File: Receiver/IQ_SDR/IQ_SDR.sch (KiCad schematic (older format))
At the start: 97 parts, among them CON1 SJ1-3523N, J1 ANT, J10 LO_I, J11 LO_Q, J12 GNDA, J13 I_IN, J14 Q_IN, J15 +5V, J16 4.3V, J17 I_OUT, J18 Q_OUT, J19 Conn_01x01_Male, J2 GND, J20 Conn_01x01_Male, J3 V_IN pin header, J4 GND, J5 V_IN, J6 FIL_O, J7 CLK1, J8 CLK2, J9 CLK0, P1 BNC, P2 SMA, Q1 MMBT2222A-TP, T1 Transformer_1P_SS, U1 FST3253 or TS3A5017, U2 Si5351A-B-GT, U3 TS5A23157, U4 LM4562 or LT6231, U5 74ALVC74D, Y1 CX3225

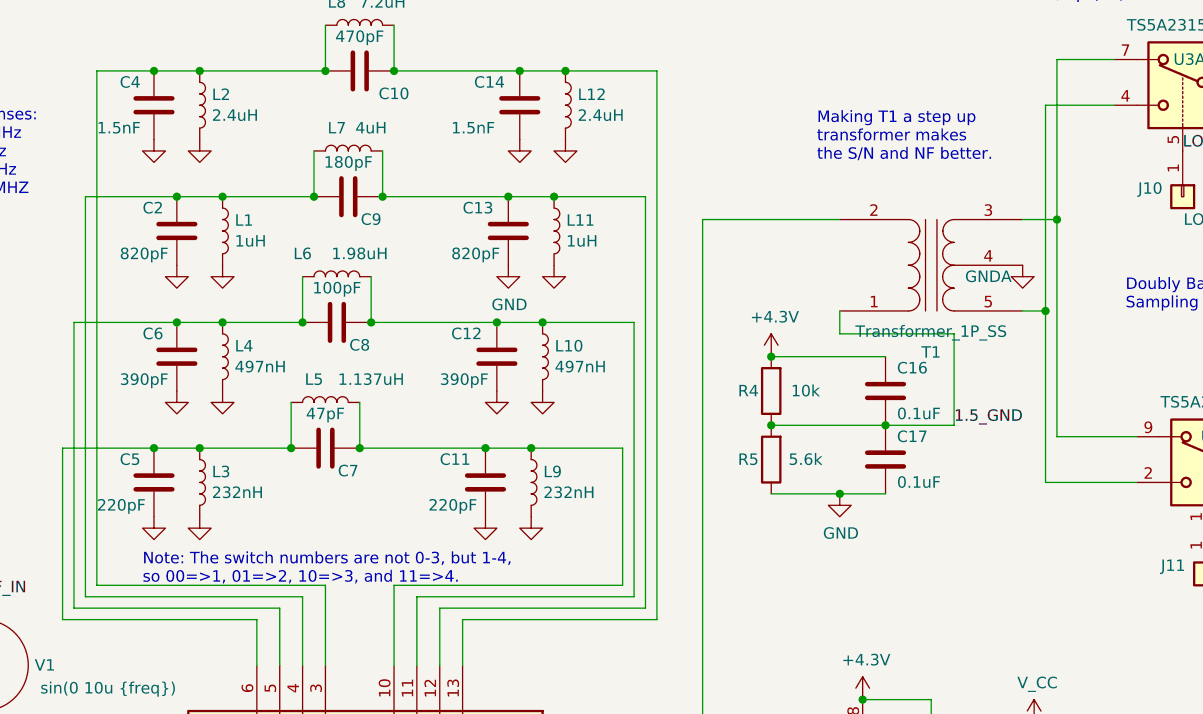
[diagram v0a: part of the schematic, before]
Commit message: Fixes to band pass filters, and notes to help with software.
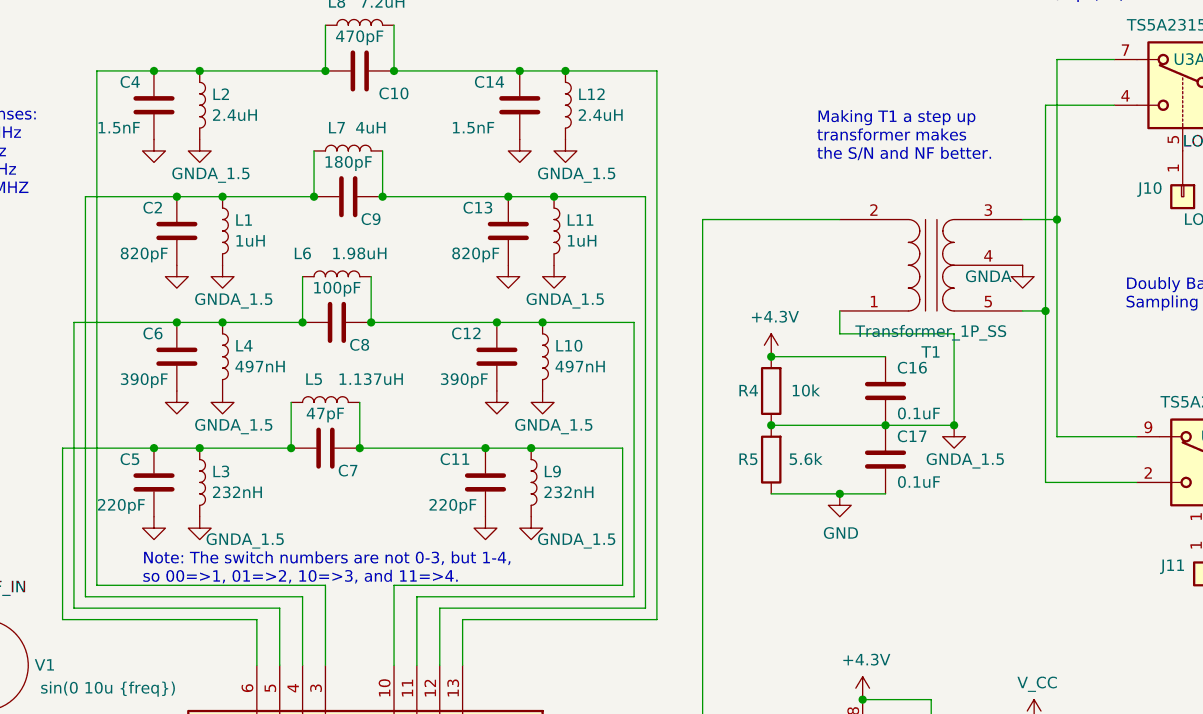
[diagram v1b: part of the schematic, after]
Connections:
- net 1.5_GND is gone; now on net GNDA: C16.2, C17.1, R4.1, R5.2, T1.1 (AA)
- net GND: no longer L1.2, L10.2, L11.2, L12.2, L2.2, L3.2, L4.2, L9.2
- net GNDA: now also L1.2, L10.2, L11.2, L12.2, L2.2, L3.2, L4.2, L9.2
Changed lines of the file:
@@
-$EndComp
-$Comp
-L IQ_SDR-rescue:GND-power #PWR016
-U 1 1 5D18958A
-P 2000 3900
-F 0 "#PWR016" H 2000 3650 50  0001 C CNN
-F 1 "GND" H 2005 3727 50  0001 C CNN
-F 2 "" H 2000 3900 50  0001 C CNN
-F 3 "" H 2000 3900 50  0001 C CNN
-	1    2000 3900
-	1    0    0    -1
 $EndComp
 $Comp
@@
 F 3 "" H 3400 3900 50  0001 C CNN
 	1    3400 3900
-	1    0    0    -1
-$EndComp
-$Comp
-L IQ_SDR-rescue:GND-power #PWR031
-U 1 1 5D189714
-P 3600 3900
-F 0 "#PWR031" H 3600 3650 50  0001 C CNN
-F 1 "GND" H 3605 3727 50  0001 C CNN
-F 2 "" H 3600 3900 50  0001 C CNN
-F 3 "" H 3600 3900 50  0001 C CNN
-	1    3600 3900
 	1    0    0    -1
 $EndComp
@@
 $EndComp
 $Comp
-L IQ_SDR-rescue:GND-power #PWR015
-U 1 1 5D1D4024
-P 2100 4450
-F 0 "#PWR015" H 2100 4200 50  0001 C CNN
-F 1 "GND" H 2105 4277 50  0001 C CNN
-F 2 "" H 2100 4450 50  0001 C CNN
-F 3 "" H 2100 4450 50  0001 C CNN
-	1    2100 4450
-	1    0    0    -1
-$EndComp
-$Comp
 L IQ_SDR-rescue:GND-power #PWR025
 U 1 1 5D1D402A
 P 3350 4450
 F 0 "#PWR025" H 3350 4200 50  0001 C CNN
-F 1 "GND" H 3355 4277 50  0000 C CNN
+F 1 "GND-power" H 3355 4277 50  0001 C CNN
 F 2 "" H 3350 4450 50  0001 C CNN
 F 3 "" H 3350 4450 50  0001 C CNN
 	1    3350 4450
-	1    0    0    -1
-$EndComp
-$Comp
-L IQ_SDR-rescue:GND-power #PWR030
-U 1 1 5D1D4030
-P 3550 4450
-F 0 "#PWR030" H 3550 4200 50  0001 C CNN
-F 1 "GND" H 3555 4277 50  0001 C CNN
-F 2 "" H 3550 4450 50  0001 C CNN
-F 3 "" H 3550 4450 50  0001 C CNN
-	1    3550 4450
 	1    0    0    -1
 $EndComp
@@
 $EndComp
 $Comp
-L IQ_SDR-rescue:GND-power #PWR018
-U 1 1 5D22E34C
-P 2100 5000
-F 0 "#PWR018" H 2100 4750 50  0001 C CNN
-F 1 "GND" H 2105 4827 50  0001 C CNN
-F 2 "" H 2100 5000 50  0001 C CNN
-F 3 "" H 2100 5000 50  0001 C CNN
-	1    2100 5000
-	1    0    0    -1
-$EndComp
-$Comp
 L IQ_SDR-rescue:GND-power #PWR024
 U 1 1 5D22E352
@@
 F 3 "" H 3300 5000 50  0001 C CNN
 	1    3300 5000
-	1    0    0    -1
-$EndComp
-$Comp
-L IQ_SDR-rescue:GND-power #PWR029
-U 1 1 5D22E358
-P 3500 5000
-F 0 "#PWR029" H 3500 4750 50  0001 C CNN
-F 1 "GND" H 3505 4827 50  0001 C CNN
-F 2 "" H 3500 5000 50  0001 C CNN
-F 3 "" H 3500 5000 50  0001 C CNN
-	1    3500 5000
 	1    0    0    -1
 $EndComp
@@
 $EndComp
 $Comp
-L IQ_SDR-rescue:GND-power #PWR017
-U 1 1 5D258FF6
-P 2000 5550
-F 0 "#PWR017" H 2000 5300 50  0001 C CNN
-F 1 "GND" H 2005 5377 50  0001 C CNN
-F 2 "" H 2000 5550 50  0001 C CNN
-F 3 "" H 2000 5550 50  0001 C CNN
-	1    2000 5550
-	1    0    0    -1
-$EndComp
-$Comp
 L IQ_SDR-rescue:GND-power #PWR023
 U 1 1 5D258FFC
@@
 F 3 "" H 3250 5550 50  0001 C CNN
 	1    3250 5550
-	1    0    0    -1
-$EndComp
-$Comp
-L IQ_SDR-rescue:GND-power #PWR027
-U 1 1 5D259002
-P 3450 5550
-F 0 "#PWR027" H 3450 5300 50  0001 C CNN
-F 1 "GND" H 3455 5377 50  0001 C CNN
-F 2 "" H 3450 5550 50  0001 C CNN
-F 3 "" H 3450 5550 50  0001 C CNN
-	1    3450 5550
 	1    0    0    -1
 $EndComp
@@
 Text Notes 1750 5850 0    50   ~ 0
 Note: The switch numbers are not 0-3, but 1-4,\nso 00=>1, 01=>2, 10=>3, and 11=>4.
-Text Label 5300 5150 0    50   ~ 0
-1.5_GND
 Text Notes 1700 3250 0    50   ~ 0
 Inductors in bandpass filters need to go to 1.5_GND, not GND.\nThey will short out the bias for the switches.
+$Comp
+L IQ_SDR-rescue:GNDA_1.5 #PWR?
+U 1 1 5DFD18B6
+P 3450 5550
+F 0 "#PWR?" H 3450 5300 50  0001 C CNN
+F 1 "GNDA_1.5" H 3650 5450 50  0000 C CNN
+F 2 "" H 3450 5550 50  0001 C CNN
+F 3 "" H 3450 5550 50  0001 C CNN
+	1    3450 5550
+	1    0    0    -1
+$EndComp
+$Comp
+L IQ_SDR-rescue:GNDA_1.5 #PWR?
+U 1 1 5DFD20EC
+P 2000 5550
+F 0 "#PWR?" H 2000 5300 50  0001 C CNN
+F 1 "GNDA_1.5" H 2200 5450 50  0000 C CNN
+F 2 "" H 2000 5550 50  0001 C CNN
+F 3 "" H 2000 5550 50  0001 C CNN
+	1    2000 5550
+	1    0    0    -1
+$EndComp
+$Comp
+L IQ_SDR-rescue:GNDA_1.5 #PWR?
+U 1 1 5DFD2615
+P 2100 5000
+F 0 "#PWR?" H 2100 4750 50  0001 C CNN
+F 1 "GNDA_1.5" H 2150 4850 50  0000 C CNN
+F 2 "" H 2100 5000 50  0001 C CNN
+F 3 "" H 2100 5000 50  0001 C CNN
+	1    2100 5000
+	1    0    0    -1
+$EndComp
+$Comp
+L IQ_SDR-rescue:GNDA_1.5 #PWR?
+U 1 1 5DFD2B56
+P 3500 5000
+F 0 "#PWR?" H 3500 4750 50  0001 C CNN
+F 1 "GNDA_1.5" H 3550 4850 50  0000 C CNN
+F 2 "" H 3500 5000 50  0001 C CNN
+F 3 "" H 3500 5000 50  0001 C CNN
+	1    3500 5000
+	1    0    0    -1
+$EndComp
+$Comp
+L IQ_SDR-rescue:GNDA_1.5 #PWR?
+U 1 1 5DFE0E2F
+P 3550 4450
+F 0 "#PWR?" H 3550 4200 50  0001 C CNN
+F 1 "GNDA_1.5" H 3600 4300 50  0000 C CNN
+F 2 "" H 3550 4450 50  0001 C CNN
+F 3 "" H 3550 4450 50  0001 C CNN
+	1    3550 4450
+	1    0    0    -1
+$EndComp
+$Comp
+L IQ_SDR-rescue:GNDA_1.5 #PWR?
+U 1 1 5DFE128D
+P 2100 4450
+F 0 "#PWR?" H 2100 4200 50  0001 C CNN
+F 1 "GNDA_1.5" H 2150 4300 50  0000 C CNN
+F 2 "" H 2100 4450 50  0001 C CNN
+F 3 "" H 2100 4450 50  0001 C CNN
+	1    2100 4450
+	1    0    0    -1
+$EndComp
+$Comp
+L IQ_SDR-rescue:GNDA_1.5 #PWR?
+U 1 1 5DFE192D
+P 3600 3900
+F 0 "#PWR?" H 3600 3650 50  0001 C CNN
+F 1 "GNDA_1.5" H 3650 3750 50  0000 C CNN
+F 2 "" H 3600 3900 50  0001 C CNN
+F 3 "" H 3600 3900 50  0001 C CNN
+	1    3600 3900
+	1    0    0    -1
+$EndComp
+$Comp
+L IQ_SDR-rescue:GNDA_1.5 #PWR?
+U 1 1 5DFE1C8B
+P 2000 3900
+F 0 "#PWR?" H 2000 3650 50  0001 C CNN
+F 1 "GNDA_1.5" H 2050 3750 50  0000 C CNN
+F 2 "" H 2000 3900 50  0001 C CNN
+F 3 "" H 2000 3900 50  0001 C CNN
+	1    2000 3900
+	1    0    0    -1
+$EndComp
+$Comp
+L IQ_SDR-rescue:GNDA_1.5 #PWR?
+U 1 1 5DFE2205
+P 5300 5150
+F 0 "#PWR?" H 5300 4900 50  0001 C CNN
+F 1 "GNDA_1.5" H 5350 5000 50  0000 C CNN
+F 2 "" H 5300 5150 50  0001 C CNN
+F 3 "" H 5300 5150 50  0001 C CNN
+	1    5300 5150
+	1    0    0    -1
+$EndComp
+Connection ~ 5300 5150
 $EndSCHEMATC

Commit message: Fixed R9-R12 and C26 and C26-C27 values
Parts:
- C26, C27: value 2200pF -> 440pF
- R10, R9: value 10 -> 51
- R11, R12: value 1.0k -> 5.1k
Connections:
- wire segments 216 -> 217
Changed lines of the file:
@@
 Title "Arduino HF SDR Receiver"
 Date "2019-07-11"
-Rev "0.1"
+Rev "0.11"
 Comp "Walla Walla University"
 Comment1 "Rob Frohne, KL7NA"
@@
 P 9550 1950
 F 0 "A1" H 9550 1900 50  0000 C CNN
-F 1 "Arduino_Nano_v3.x" H 9650 650 50  0000 C CNN
+F 1 "Arduino_Nano_v3.x" H 9550 2650 50  0000 C CNN
 F 2 "Modules:Arduino_Nano" H 9700 1000 50  0001 L CNN
 F 3 "https://www.arduino.cc/en/uploads/Main/Arduino_Nano-Rev3.2-SCH.pdf" H 9550 950 50  0001 C CNN
@@
 LO_Q
 $Comp
-L IQ_SDR-rescue:GNDA-power #PWR042
-U 1 1 5CF5C6F9
-P 5600 4450
-F 0 "#PWR042" H 5600 4200 50  0001 C CNN
-F 1 "GNDA" H 5450 4400 50  0000 C CNN
-F 2 "" H 5600 4450 50  0001 C CNN
-F 3 "" H 5600 4450 50  0001 C CNN
-	1    5600 4450
-	1    0    0    -1
-$EndComp
-$Comp
 L IQ_SDR-rescue:+3.3V-power #PWR040
 U 1 1 5CF636F6
@@
 $EndComp
 $Comp
-L IQ_SDR-rescue:GNDA-power #PWR055
-U 1 1 5D491346
-P 7750 4600
-F 0 "#PWR055" H 7750 4350 50  0001 C CNN
-F 1 "GNDA" H 7755 4427 50  0000 C CNN
-F 2 "" H 7750 4600 50  0001 C CNN
-F 3 "" H 7750 4600 50  0001 C CNN
-	1    7750 4600
-	1    0    0    -1
-$EndComp
-$Comp
 L IQ_SDR-rescue:GND-power #PWR053
 U 1 1 5CFD92C7
@@
 	7750 4600 7750 4250
 Wire Wire Line
-	7750 3850 8200 3850
+	7750 3850 7950 3850
 Connection ~ 7750 4250
-$Comp
-L IQ_SDR-rescue:GNDA-power #PWR059
-U 1 1 5D491349
-P 8200 5250
-F 0 "#PWR059" H 8200 5000 50  0001 C CNN
-F 1 "GNDA" H 8205 5077 50  0000 C CNN
-F 2 "" H 8200 5250 50  0001 C CNN
-F 3 "" H 8200 5250 50  0001 C CNN
-	1    8200 5250
-	1    0    0    -1
-$EndComp
 $Comp
 L IQ_SDR-rescue:C-Device C22
@@
 P 7900 5050
 F 0 "R10" V 7693 5050 50  0000 C CNN
-F 1 "10" V 7784 5050 50  0000 C CNN
+F 1 "51" V 7784 5050 50  0000 C CNN
 F 2 "Resistors_SMD:R_0805" V 7830 5050 50  0001 C CNN
 F 3 "~" H 7900 5050 50  0001 C CNN
@@
 P 8500 4700
 F 0 "R12" V 8293 4700 50  0000 C CNN
-F 1 "1.0k" V 8384 4700 50  0000 C CNN
+F 1 "5.1k" V 8384 4700 50  0000 C CNN
 F 2 "Resistors_SMD:R_0805" V 8430 4700 50  0001 C CNN
 F 3 "~" H 8500 4700 50  0001 C CNN
@@
 P 8500 4350
 F 0 "C27" V 8450 4500 50  0000 C CNN
-F 1 "2200pF" V 8350 4350 50  0000 C CNN
+F 1 "440pF" V 8350 4350 50  0000 C CNN
 F 2 "Capacitors_SMD:C_0805" H 8538 4200 50  0001 C CNN
 F 3 "~" H 8500 4350 50  0001 C CNN
@@
 P 7850 3650
 F 0 "R9" V 7643 3650 50  0000 C CNN
-F 1 "10" V 7734 3650 50  0000 C CNN
+F 1 "51" V 7734 3650 50  0000 C CNN
 F 2 "Resistors_SMD:R_0805" V 7780 3650 50  0001 C CNN
 F 3 "~" H 7850 3650 50  0001 C CNN
@@
 P 8500 3300
 F 0 "R11" V 8293 3300 50  0000 C CNN
-F 1 "1.0k" V 8384 3300 50  0000 C CNN
+F 1 "5.1k" V 8384 3300 50  0000 C CNN
 F 2 "Resistors_SMD:R_0805" V 8430 3300 50  0001 C CNN
 F 3 "~" H 8500 3300 50  0001 C CNN
@@
 P 8500 2950
 F 0 "C26" V 8450 3200 50  0000 C CNN
-F 1 "2200pF" V 8450 2750 50  0000 C CNN
+F 1 "440pF" V 8450 2750 50  0000 C CNN
 F 2 "Capacitors_SMD:C_0805" H 8538 2800 50  0001 C CNN
 F 3 "~" H 8500 2950 50  0001 C CNN
@@
 $EndComp
 Connection ~ 1400 7250
-Connection ~ 8200 5250
 Wire Wire Line
 	6750 3650 7050 3650
@@
 U 1 1 5D296A71
 P 4900 1350
-F 0 "J9" V 4864 1262 50  0000 R CNN
+F 0 "J9" V 4900 1250 50  0000 R CNN
 F 1 "CLK0" V 5000 1450 50  0000 R CNN
 F 2 "Connectors:PINTST" H 4900 1350 50  0001 C CNN
@@
 U 1 1 5CF44A30
 P 4800 1750
-F 0 "J7" H 4700 1700 50  0000 R CNN
+F 0 "J7" H 4950 1750 50  0000 R CNN
 F 1 "CLK1" H 4900 1850 50  0000 R CNN
 F 2 "Connectors:PINTST" H 4800 1750 50  0001 C CNN
@@
 U 1 1 5D491350
 P 5200 4450
-F 0 "T1" H 5200 4831 50  0000 C CNN
-F 1 "Transformer_1P_SS" H 5200 4740 50  0000 C CNN
+F 0 "T1" H 5000 4450 50  0000 C CNN
+F 1 "Transformer_1P_SS" H 5200 4150 50  0000 C CNN
 F 2 "SMA:4_to_1_Transmission_Line_TransformerTHT" H 5200 4450 50  0001 C CNN
 F 3 "~" H 5200 4450 50  0001 C CNN
@@
 P 7150 2100
 F 0 "JP1" V 7196 2012 50  0000 R CNN
-F 1 "smooth disable" V 7400 2400 50  0000 R CNN
+F 1 "smooth disable" V 7250 2750 50  0000 R CNN
 F 2 "Pin_Headers:Pin_Header_Straight_1x02_Pitch2.54mm" H 7150 2100 50  0001 C CNN
 F 3 "~" H 7150 2100 50  0001 C CNN
@@
 U 1 1 5D381DCF
 P 4600 2200
-F 0 "J20" V 4708 2244 50  0000 L CNN
+F 0 "J20" V 4650 2250 50  0000 L CNN
 F 1 "Conn_01x01_Male" V 4753 2244 50  0001 L CNN
 F 2 "Pin_Headers:Pin_Header_Straight_1x01_Pitch2.54mm" H 4600 2200 50  0001 C CNN
@@
 U 1 1 5D383943
 P 4600 2150
-F 0 "J19" V 4708 2062 50  0000 R CNN
+F 0 "J19" V 4600 2100 50  0000 R CNN
 F 1 "Conn_01x01_Male" V 4663 2062 50  0001 R CNN
 F 2 "Pin_Headers:Pin_Header_Straight_1x01_Pitch2.54mm" H 4600 2150 50  0001 C CNN
@@
 $EndComp
 Connection ~ 5300 5150
+$Comp
+L power:GNDA #PWR?
+U 1 1 5E0B56F4
+P 5600 4450
+F 0 "#PWR?" H 5600 4200 50  0001 C CNN
+F 1 "GNDA" H 5450 4350 50  0000 C CNN
+F 2 "" H 5600 4450 50  0001 C CNN
+F 3 "" H 5600 4450 50  0001 C CNN
+	1    5600 4450
+	1    0    0    -1
+$EndComp
+$Comp
+L power:GNDA #PWR?
+U 1 1 5E0B69D9
+P 7750 4600
+F 0 "#PWR?" H 7750 4350 50  0001 C CNN
+F 1 "GNDA" H 7755 4427 50  0000 C CNN
+F 2 "" H 7750 4600 50  0001 C CNN
+F 3 "" H 7750 4600 50  0001 C CNN
+	1    7750 4600
+	1    0    0    -1
+$EndComp
+$Comp
+L power:GNDA #PWR?
+U 1 1 5E0B6E6F
+P 8200 5250
+F 0 "#PWR?" H 8200 5000 50  0001 C CNN
+F 1 "GNDA" H 8205 5077 50  0000 C CNN
+F 2 "" H 8200 5250 50  0001 C CNN
+F 3 "" H 8200 5250 50  0001 C CNN
+	1    8200 5250
+	1    0    0    -1
+$EndComp
+Connection ~ 8200 5250
+$Comp
+L power:GNDA #PWR?
+U 1 1 5E0B8361
+P 7950 3850
+F 0 "#PWR?" H 7950 3600 50  0001 C CNN
+F 1 "GNDA" H 7955 3677 50  0000 C CNN
+F 2 "" H 7950 3850 50  0001 C CNN
+F 3 "" H 7950 3850 50  0001 C CNN
+	1    7950 3850
+	1    0    0    -1
+$EndComp
+Connection ~ 7950 3850
+Wire Wire Line
+	7950 3850 8200 3850
 $EndSCHEMATC

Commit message: Added a note of two things to fix
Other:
- note added: "Problems yet to solve:\nIn Quisk or maybe hardware, need to switch I and Q.\nNoise goes down significantly if USB is disconnected."
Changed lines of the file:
@@
 Connection ~ 5300 5150
 $Comp
-L power:GNDA #PWR?
+L IQ_SDR-rescue:GNDA-power #PWR?
 U 1 1 5E0B56F4
 P 5600 4450
@@
 $EndComp
 $Comp
-L power:GNDA #PWR?
+L IQ_SDR-rescue:GNDA-power #PWR?
 U 1 1 5E0B69D9
 P 7750 4600
@@
 $EndComp
 $Comp
-L power:GNDA #PWR?
+L IQ_SDR-rescue:GNDA-power #PWR?
 U 1 1 5E0B6E6F
 P 8200 5250
@@
 Connection ~ 8200 5250
 $Comp
-L power:GNDA #PWR?
+L IQ_SDR-rescue:GNDA-power #PWR?
 U 1 1 5E0B8361
 P 7950 3850
@@
 Wire Wire Line
 	7950 3850 8200 3850
+Text Notes 7500 7050 0    50   ~ 0
+Problems yet to solve:\nIn Quisk or maybe hardware, need to switch I and Q.\nNoise goes down significantly if USB is disconnected.
 $EndSCHEMATC

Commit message: Added Cern OHL
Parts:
- removed V1: sin(0 10u {freq}), symbol IQ_SDR-rescue:VSOURCE-myspice
- added JP3, JP4: Jumper, symbol Device:Jumper
- added T2: Transformer_1P_1S, symbol Device:Transformer_1P_1S
- U4: footprint SMA:DMP8 -> Housings_SOIC:SOIC-8_3.9x4.9mm_Pitch1.27mm
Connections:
- net GND: now also JP3.2, JP4.1, T2.3 (SA); no longer A1.29 (GND), A1.4 (GND), P1.2 (Ext)
- net RF_IN: now also T2.4 (SB); no longer P1.1 (In)
- new net: A1.29 (GND), A1.4 (GND), JP3.1
- new net: P1.1 (In), T2.1 (AA)
- new net: JP4.2, P1.2 (Ext), T2.2 (AB)
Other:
- note added: "For ground loops"
- note added: "Problems yet to solve:\nIn Quisk or maybe hardware, need to switch I and Q.\nOptional jumpers added to combat\nground loops without extra isolation."
- note added: "T2 for \nground \nloops.\nMay be\nunnecessary."
- note removed: "Problems yet to solve:\nIn Quisk or maybe hardware, need to switch I and Q.\nNoise goes down significantly if USB is disconnected."
- moved on the sheet: C1, C10, C11, C12, C13, C14, C2, C3, C4, C5, C6, C7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
